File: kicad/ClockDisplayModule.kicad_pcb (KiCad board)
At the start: 2 copper layers, 88.9 x 54.6 mm, 39 parts, among them IC101 ATMEGA8-P, P101 CONN_02X03, P102 CONN_01X05, P201 CONN_01X06, P202 CONN_01X07, P203 CONN_01X06, P204 CONN_01X07, Q201 BC856BS, Q202 BC856BS, Q203 BC856BS, U201 SN74LS138, U202 74HC4511

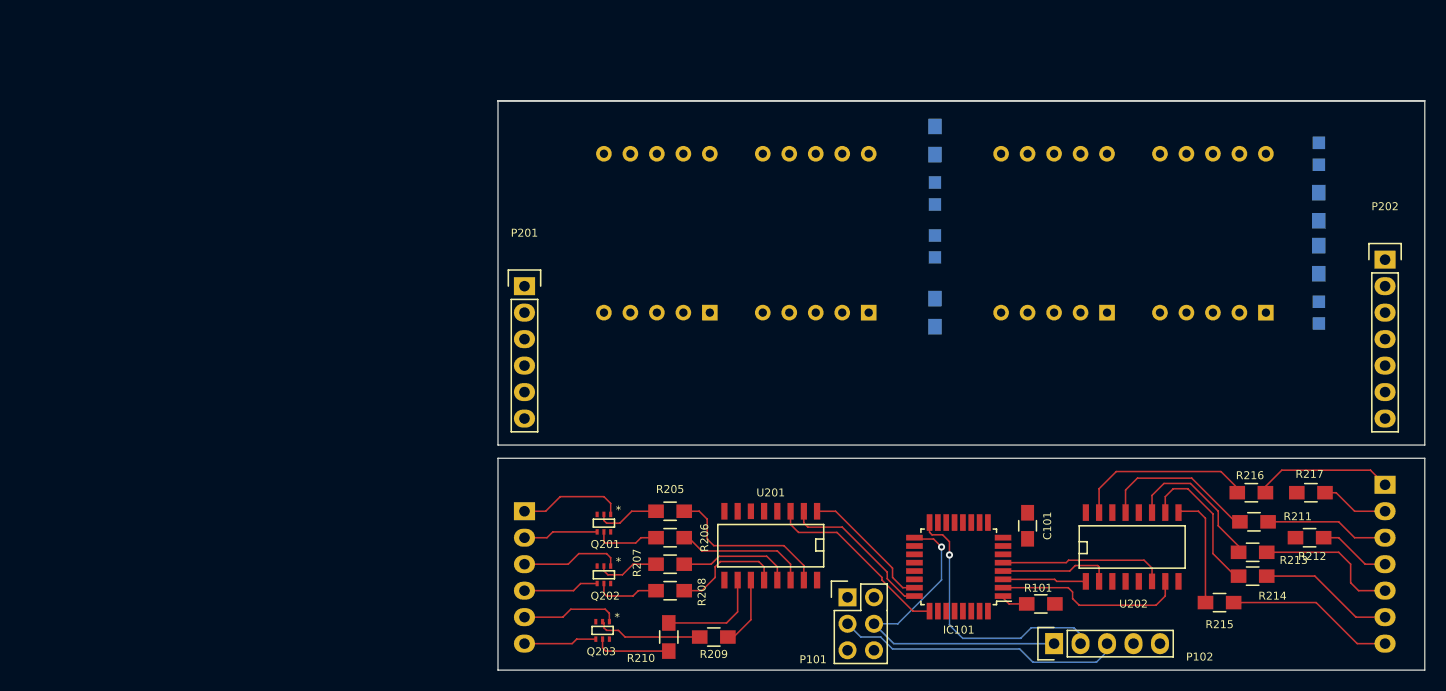
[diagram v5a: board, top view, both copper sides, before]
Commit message: Board layout completed
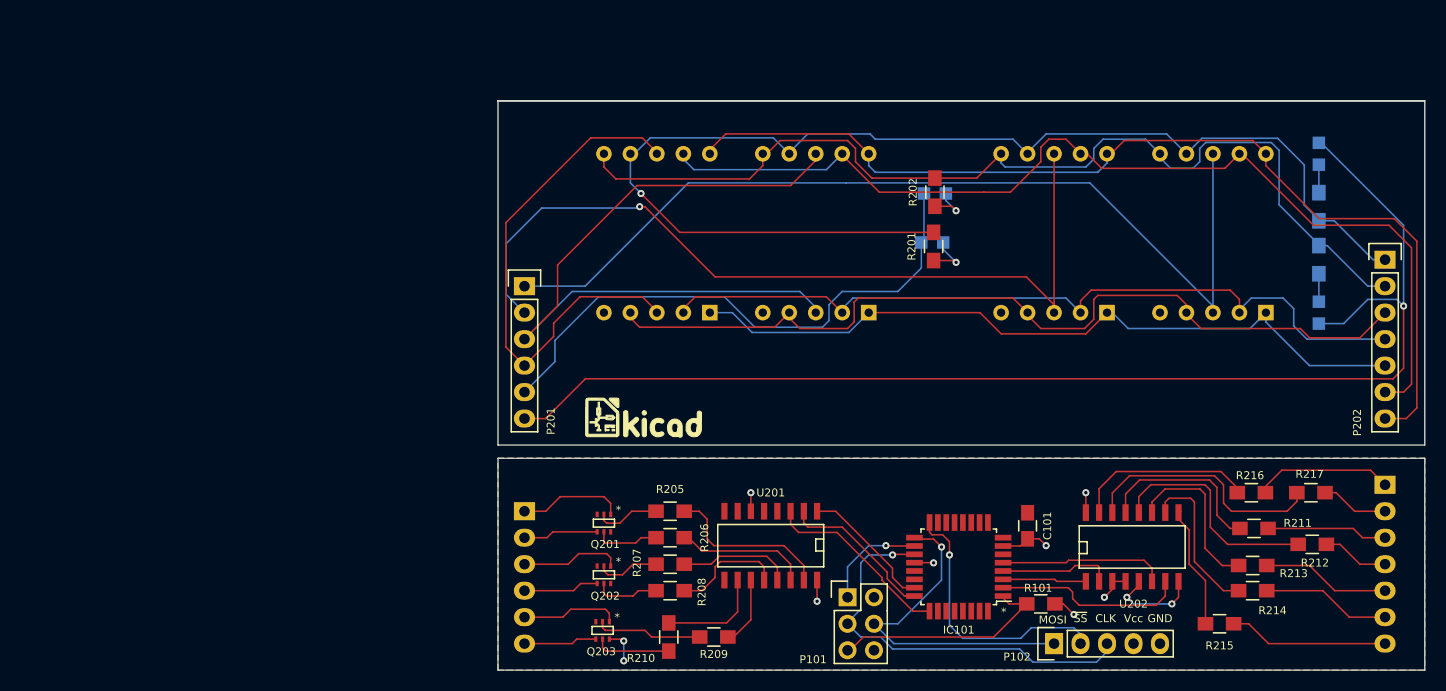
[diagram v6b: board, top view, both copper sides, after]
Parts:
- added G***: LOGO, ClockFootprints:kicad_logo, F.Cu at (130.8, 73.5)
- R201, R202: moved to F.Cu
- moved R201 6.35 mm to (158.6, 57.1), turned to 90 degrees
- moved R202 4.95 mm to (158.8, 51.9), turned to 90 degrees
- moved R215 2.03 mm to (186.1, 93.3)
- moved R214 1.40 mm to (189.2, 90.2)
- moved R213 1.27 mm to (189.2, 87.8)
- moved R212 0.68 mm to (194.9, 85.7)
- moved R211 0.63 mm to (189.4, 84.2)
- moved D201 0.46 mm to (158.5, 56.8), turned to 0 degrees
- turned D202 to 0 degrees
- turned D203 to 270 degrees
- turned R203 to 270 degrees
- turned R204 to 90 degrees
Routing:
- net D_Signal: track 0.00 -> 120.8 mm, vias 0 -> 1
- net /Display Driver/Seg_A: track 0.00 -> 120.0 mm, vias 0 -> 1
- net /Display Driver/Seg_F: track 0.00 -> 99.1 mm
- net /Display Driver/Seg_G: track 0.00 -> 98.9 mm
- net /Display Driver/Seg_B: track 0.00 -> 97.7 mm
- net D_Dig_0: track 0.00 -> 90.9 mm
- net /Display Driver/Seg_C: track 0.00 -> 84.4 mm
- net D_Dig_1: track 0.00 -> 81.3 mm, vias 0 -> 1
- net /Display Driver/Seg_D: track 0.00 -> 77.2 mm
- net /Display Driver/Seg_E: track 0.00 -> 72.6 mm
- net D_Dig_2: track 0.00 -> 69.0 mm
- net D_Colon: track 0.00 -> 54.8 mm
- net D_Dig_3: track 0.00 -> 50.4 mm
- net Net-(R217-Pad2): track 0.08 -> 24.0 mm
- net Net-(R212-Pad2): track 0.00 -> 21.7 mm
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- added copper zone on F.Cu, net GND
- added copper zone on B.Cu, net VCC
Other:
- board text added: "*"
- board text added: "CLK"
- board text added: "GND"
- board text added: "MOSI"
- board text added: "Vcc"
- board text added: "~SS"

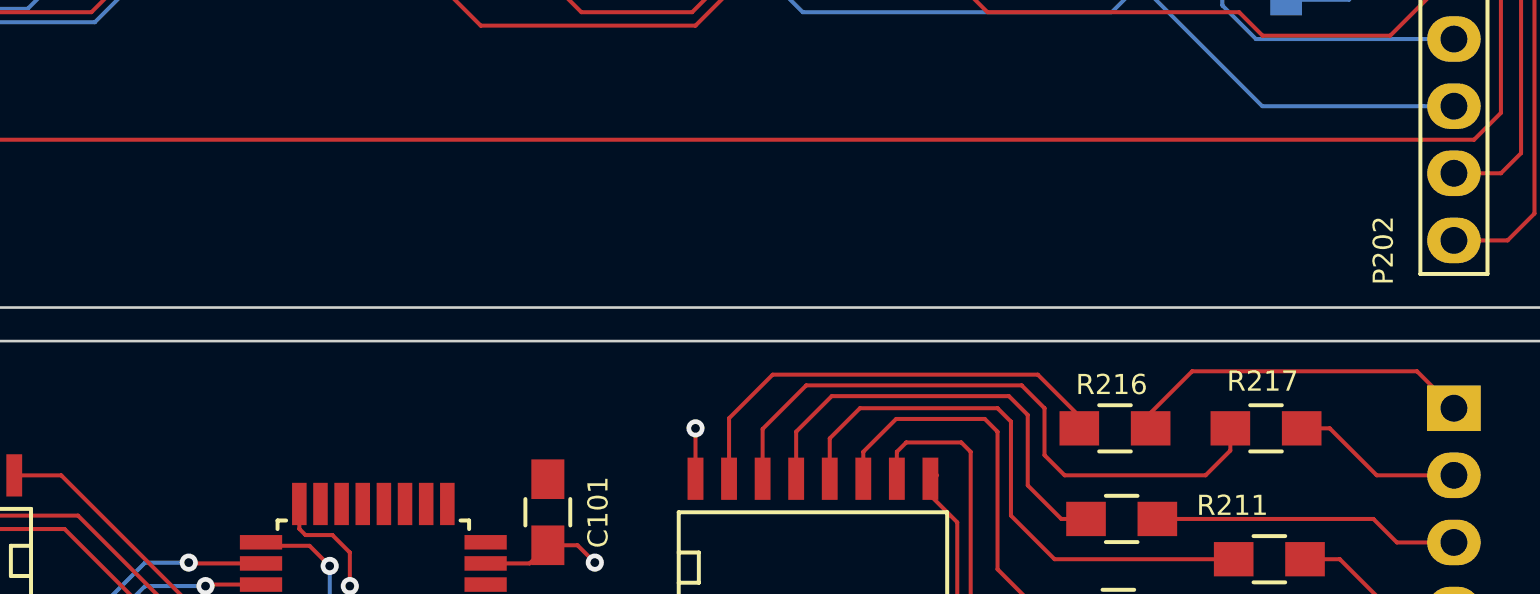
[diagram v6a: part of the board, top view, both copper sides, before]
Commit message: Added annotiations and logo
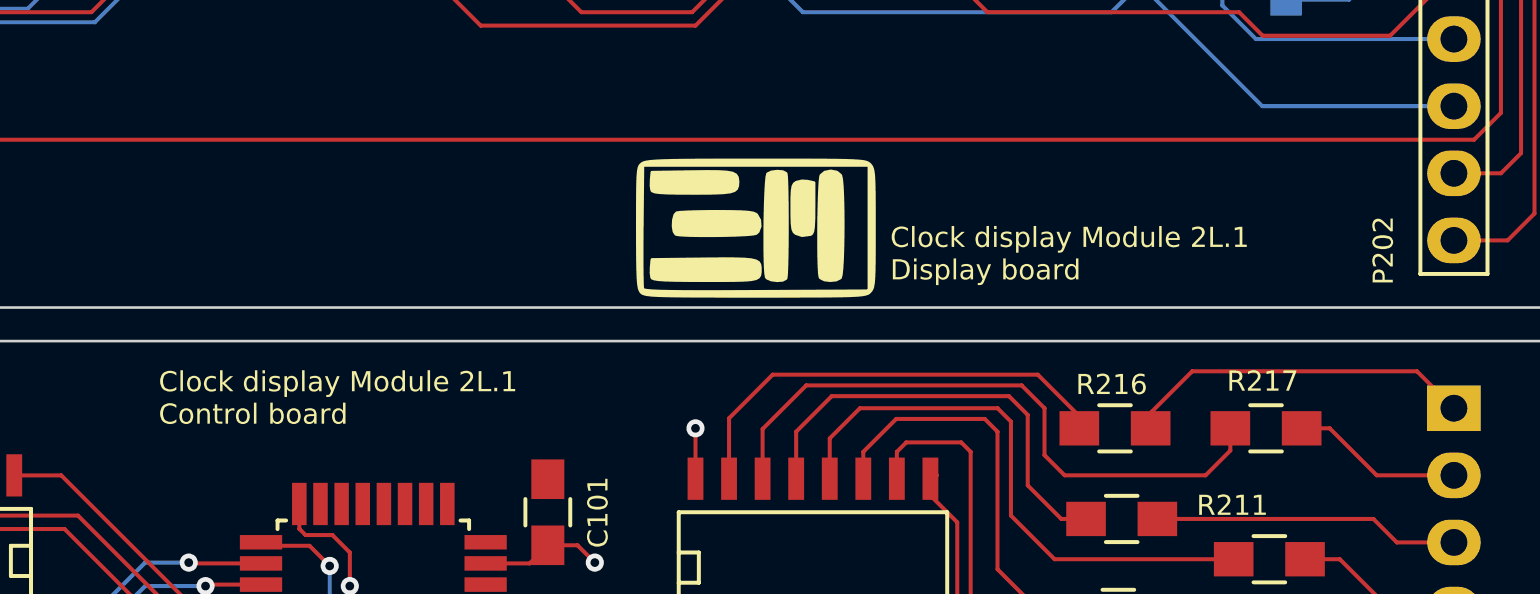
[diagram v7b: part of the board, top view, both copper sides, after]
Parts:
- added G***: LOGO, ClockFootprints:myLogo_300, F.Cu at (175.5, 73.2)
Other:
- board text added: "Clock display Module 2L.1 Control board"
- board text added: "Clock display Module 2L.1 Display board"
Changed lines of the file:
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@@
     (area 115.379501 43.079999 205.9305 97.934001)
     (thickness 1.6)
-    (drawings 18)
+    (drawings 20)
     (tracks 556)
     (zones 0)
-    (modules 40)
+    (modules 41)
     (nets 64)
   )
@@
       (xy -2.775391 0.969684)) (layer F.SilkS) (width 0.1))
   )
+  (module ClockFootprints:myLogo_300 (layer F.Cu)
+    (at 175.514 73.152)
+    (fp_text reference G*** (at 0 0) (layer F.SilkS) hide
+      (effects (font (thickness 0.3)))
+    )
+    (fp_text value LOGO (at 0.75 0) (layer F.SilkS) hide
+      (effects (font (thickness 0.3)))
+    )
+    (fp_poly (pts (xy 4.487333 0.042333) (xy 4.486735 0.718648) (xy 4.483983 1.246093) (xy 4.477641 1.645129)
+      (xy 4.466273 1.936217) (xy 4.448444 2.13982) (xy 4.422717 2.276398) (xy 4.387657 2.366412)
+      (xy 4.341828 2.430326) (xy 4.318 2.455333) (xy 4.275667 2.493018) (xy 4.275667 2.413)
+      (xy 4.275667 0.042333) (xy 4.275667 -2.328334) (xy 0 -2.328334) (xy -4.275667 -2.328334)
+      (xy -4.298254 -0.043596) (xy -4.302753 0.565419) (xy -4.303959 1.121277) (xy -4.302053 1.600765)
+      (xy -4.297218 1.980672) (xy -4.289637 2.237786) (xy -4.279492 2.348894) (xy -4.279443 2.349022)
+      (xy -4.23842 2.37407) (xy -4.128378 2.394747) (xy -3.937413 2.411292) (xy -3.653624 2.423943)
+      (xy -3.265109 2.432936) (xy -2.759964 2.438511) (xy -2.126288 2.440905) (xy -1.352177 2.440357)
+      (xy -0.425731 2.437103) (xy 0.01881 2.434951) (xy 4.275667 2.413) (xy 4.275667 2.493018)
+      (xy 4.274807 2.493784) (xy 4.219153 2.525928) (xy 4.136549 2.55233) (xy 4.012506 2.573554)
+      (xy 3.832535 2.590165) (xy 3.582146 2.602726) (xy 3.246849 2.611802) (xy 2.812157 2.617958)
+      (xy 2.263578 2.621757) (xy 1.586625 2.623765) (xy 0.766807 2.624546) (xy -0.029211 2.624666)
+      (xy -0.980068 2.624378) (xy -1.775938 2.623172) (xy -2.431164 2.620532) (xy -2.960093 2.615946)
+      (xy -3.377068 2.608897) (xy -3.696436 2.598872) (xy -3.932541 2.585357) (xy -4.099727 2.567837)
+      (xy -4.212341 2.545798) (xy -4.284726 2.518725) (xy -4.331228 2.486104) (xy -4.347211 2.469833)
+      (xy -4.389488 2.406349) (xy -4.422441 2.307356) (xy -4.447195 2.153196) (xy -4.464872 1.924211)
+      (xy -4.476598 1.600746) (xy -4.483496 1.163142) (xy -4.48669 0.591742) (xy -4.487333 0.0193)
+      (xy -4.487017 -0.663174) (xy -4.485042 -1.196181) (xy -4.479868 -1.599586) (xy -4.469954 -1.893253)
+      (xy -4.453763 -2.097049) (xy -4.429752 -2.230839) (xy -4.396383 -2.314488) (xy -4.352115 -2.367862)
+      (xy -4.299161 -2.4082) (xy -4.238619 -2.438724) (xy -4.142244 -2.464235) (xy -3.995823 -2.485167)
+      (xy -3.785141 -2.501954) (xy -3.495983 -2.51503) (xy -3.114136 -2.524828) (xy -2.625384 -2.531783)
+      (xy -2.015513 -2.536328) (xy -1.27031 -2.538897) (xy -0.375558 -2.539924) (xy 0.018839 -2.54)
+      (xy 0.96181 -2.539804) (xy 1.750028 -2.538833) (xy 2.398073 -2.536512) (xy 2.920525 -2.532267)
+      (xy 3.331965 -2.525524) (xy 3.646972 -2.515709) (xy 3.880126 -2.502247) (xy 4.046008 -2.484564)
+      (xy 4.159198 -2.462085) (xy 4.234276 -2.434238) (xy 4.285823 -2.400446) (xy 4.318 -2.370667)
+      (xy 4.368997 -2.311742) (xy 4.408597 -2.235676) (xy 4.438234 -2.122008) (xy 4.459345 -1.950276)
+      (xy 4.473366 -1.700019) (xy 4.481732 -1.350776) (xy 4.485879 -0.882084) (xy 4.487244 -0.273483)
+      (xy 4.487333 0.042333) (xy 4.487333 0.042333)) (layer F.SilkS) (width 0.1))
+    (fp_poly (pts (xy 0.169333 1.569775) (xy 0.168358 1.713093) (xy 0.152319 1.823251) (xy 0.101542 1.904606)
+      (xy -0.003646 1.961519) (xy -0.182918 1.998349) (xy -0.455948 2.019454) (xy -0.842407 2.029194)
+      (xy -1.361969 2.031928) (xy -1.916716 2.032) (xy -2.565158 2.030372) (xy -3.063014 2.024757)
+      (xy -3.429009 2.014057) (xy -3.681865 1.997174) (xy -3.840307 1.973011) (xy -3.923057 1.94047)
+      (xy -3.945623 1.913059) (xy -3.969714 1.749515) (xy -3.964863 1.518743) (xy -3.964132 1.510893)
+      (xy -3.937 1.227666) (xy -2.00029 1.204883) (xy -1.33821 1.198616) (xy -0.82622 1.199461)
+      (xy -0.445124 1.210647) (xy -0.175723 1.235403) (xy 0.001181 1.276957) (xy 0.104785 1.338538)
+      (xy 0.154287 1.423375) (xy 0.168885 1.534697) (xy 0.169333 1.569775) (xy 0.169333 1.569775)) (layer F.SilkS) (width 0.1))
+    (fp_poly (pts (xy 1.193668 0.120363) (xy 1.190669 0.619662) (xy 1.184541 1.07985) (xy 1.175312 1.471151)
+      (xy 1.163005 1.763794) (xy 1.147647 1.928005) (xy 1.141157 1.950315) (xy 1.016335 2.017821)
+      (xy 0.806727 2.035325) (xy 0.584974 2.007877) (xy 0.423718 1.940532) (xy 0.390058 1.898075)
+      (xy 0.365742 1.749654) (xy 0.348343 1.469809) (xy 0.337475 1.088532) (xy 0.332753 0.635815)
+      (xy 0.333793 0.14165) (xy 0.340209 -0.363972) (xy 0.351618 -0.851058) (xy 0.367634 -1.289618)
+      (xy 0.387873 -1.649658) (xy 0.411949 -1.901188) (xy 0.439478 -2.014215) (xy 0.440267 -2.015067)
+      (xy 0.592465 -2.086693) (xy 0.811553 -2.11396) (xy 1.021119 -2.095305) (xy 1.144557 -2.029481)
+      (xy 1.160858 -1.920749) (xy 1.173879 -1.672489) (xy 1.183645 -1.314474) (xy 1.190182 -0.876479)
+      (xy 1.193514 -0.388275) (xy 1.193668 0.120363) (xy 1.193668 0.120363)) (layer F.SilkS) (width 0.1))
+    (fp_poly (pts (xy 3.305389 -0.208451) (xy 3.303391 0.296811) (xy 3.294913 0.783229) (xy 3.280065 1.220386)
+      (xy 3.258955 1.577866) (xy 3.231693 1.825256) (xy 3.2004 1.9304) (xy 3.038356 2.008924)
+      (xy 2.81175 2.032997) (xy 2.589751 2.005491) (xy 2.441525 1.92928) (xy 2.422058 1.898075)
+      (xy 2.400118 1.754847) (xy 2.384222 1.476565) (xy 2.374077 1.094413) (xy 2.369388 0.63958)
+      (xy 2.369862 0.143252) (xy 2.375206 -0.363385) (xy 2.385126 -0.849145) (xy 2.399329 -1.282841)
+      (xy 2.41752 -1.633286) (xy 2.439406 -1.869293) (xy 2.458312 -1.9529) (xy 2.610192 -2.080148)
+      (xy 2.835527 -2.122755) (xy 3.061111 -2.080722) (xy 3.213735 -1.954048) (xy 3.214354 -1.9529)
+      (xy 3.246395 -1.809644) (xy 3.27141 -1.533155) (xy 3.289508 -1.15385) (xy 3.300797 -0.702144)
+      (xy 3.305389 -0.208451) (xy 3.305389 -0.208451)) (layer F.SilkS) (width 0.1))
+    (fp_poly (pts (xy 0.162789 -0.021957) (xy 0.086615 0.179943) (xy 0.005566 0.251021) (xy -0.125287 0.276844)
+      (xy -0.389757 0.29824) (xy -0.752176 0.314839) (xy -1.176879 0.326269) (xy -1.628196 0.332158)
+      (xy -2.07046 0.332135) (xy -2.468005 0.325829) (xy -2.785162 0.312869) (xy -2.986265 0.292882)
+      (xy -3.026833 0.282593) (xy -3.103765 0.172081) (xy -3.135243 -0.033446) (xy -3.123566 -0.266543)
+      (xy -3.071033 -0.459764) (xy -2.998742 -0.541275) (xy -2.87182 -0.55863) (xy -2.607337 -0.573481)
+      (xy -2.23706 -0.584753) (xy -1.792753 -0.591371) (xy -1.48079 -0.592667) (xy -0.94731 -0.590103)
+      (xy -0.558048 -0.580945) (xy -0.287944 -0.562996) (xy -0.111939 -0.534059) (xy -0.004975 -0.491934)
+      (xy 0.036286 -0.45962) (xy 0.147033 -0.258763) (xy 0.162789 -0.021957) (xy 0.162789 -0.021957)) (layer F.SilkS) (width 0.1))
+    (fp_poly (pts (xy 2.201333 -0.721998) (xy 2.197621 -0.294621) (xy 2.183958 -0.007902) (xy 2.156553 0.16672)
+      (xy 2.111618 0.257808) (xy 2.067408 0.287274) (xy 1.743921 0.328897) (xy 1.502833 0.247218)
+      (xy 1.434938 0.184455) (xy 1.391145 0.069716) (xy 1.366519 -0.129238) (xy 1.356127 -0.444646)
+      (xy 1.354667 -0.720895) (xy 1.357492 -1.120044) (xy 1.36996 -1.38341) (xy 1.398062 -1.544504)
+      (xy 1.447788 -1.636838) (xy 1.525128 -1.693922) (xy 1.528966 -1.695991) (xy 1.738999 -1.746947)
+      (xy 1.952299 -1.734576) (xy 2.201333 -1.679879) (xy 2.201333 -0.721998) (xy 2.201333 -0.721998)) (layer F.SilkS) (width 0.1))
+    (fp_poly (pts (xy -0.677333 -1.6999) (xy -0.686016 -1.554442) (xy -0.726477 -1.446051) (xy -0.820334 -1.369302)
+      (xy -0.989207 -1.318769) (xy -1.254715 -1.289027) (xy -1.638476 -1.274649) (xy -2.162109 -1.27021)
+      (xy -2.390257 -1.27) (xy -2.949843 -1.272386) (xy -3.361312 -1.28062) (xy -3.64583 -1.296323)
+      (xy -3.82456 -1.321111) (xy -3.918667 -1.356605) (xy -3.945623 -1.388941) (xy -3.969714 -1.552485)
+      (xy -3.964863 -1.783257) (xy -3.964132 -1.791107) (xy -3.937 -2.074334) (xy -2.424079 -2.097495)
+      (xy -1.83755 -2.104034) (xy -1.398932 -2.099974) (xy -1.086901 -2.080461) (xy -0.880132 -2.040642)
+      (xy -0.757301 -1.975662) (xy -0.697083 -1.880668) (xy -0.678154 -1.750806) (xy -0.677333 -1.6999)
+      (xy -0.677333 -1.6999)) (layer F.SilkS) (width 0.1))
+  )
+  (gr_text "Clock display Module 2L.1\nControl board" (at 152.908 79.629) (layer F.SilkS)
+    (effects (font (size 0.762 0.762) (thickness 0.127)) (justify left))
+  )
+  (gr_text "Clock display Module 2L.1\nDisplay board" (at 180.594 74.168) (layer F.SilkS)
+    (effects (font (size 0.762 0.762) (thickness 0.127)) (justify left))
+  )
   (gr_text * (at 165.354 92.202) (layer F.SilkS)

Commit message: refined the logo image
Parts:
- removed the G*** at (175.5, 73.2)
- added G***: LOGO, ClockFootprints:myLogo_600, F.Cu at (175.6, 72.9)
